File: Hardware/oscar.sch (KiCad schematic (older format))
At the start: 49 parts, among them J1 SWD_Header, J2 ChannelA_In, J3 ChannelB_In, J4 ChannelC_In, J5 ChA_Buff_Out, J6 ChB_Buff_Out, J7 ChC_Buff_Out, J8 MIDI_In, J9 Eurorack_10_pin_power, SW1 Left_Encoder, SW2 Right_Encoder, SW3 SW_Push, U1 STM32F446RETx, U2 ILI9341_SPI_Daughterboard, U3 MCP6004, U4 TL074, U5 LM1117-3.3, Y1 Crystal

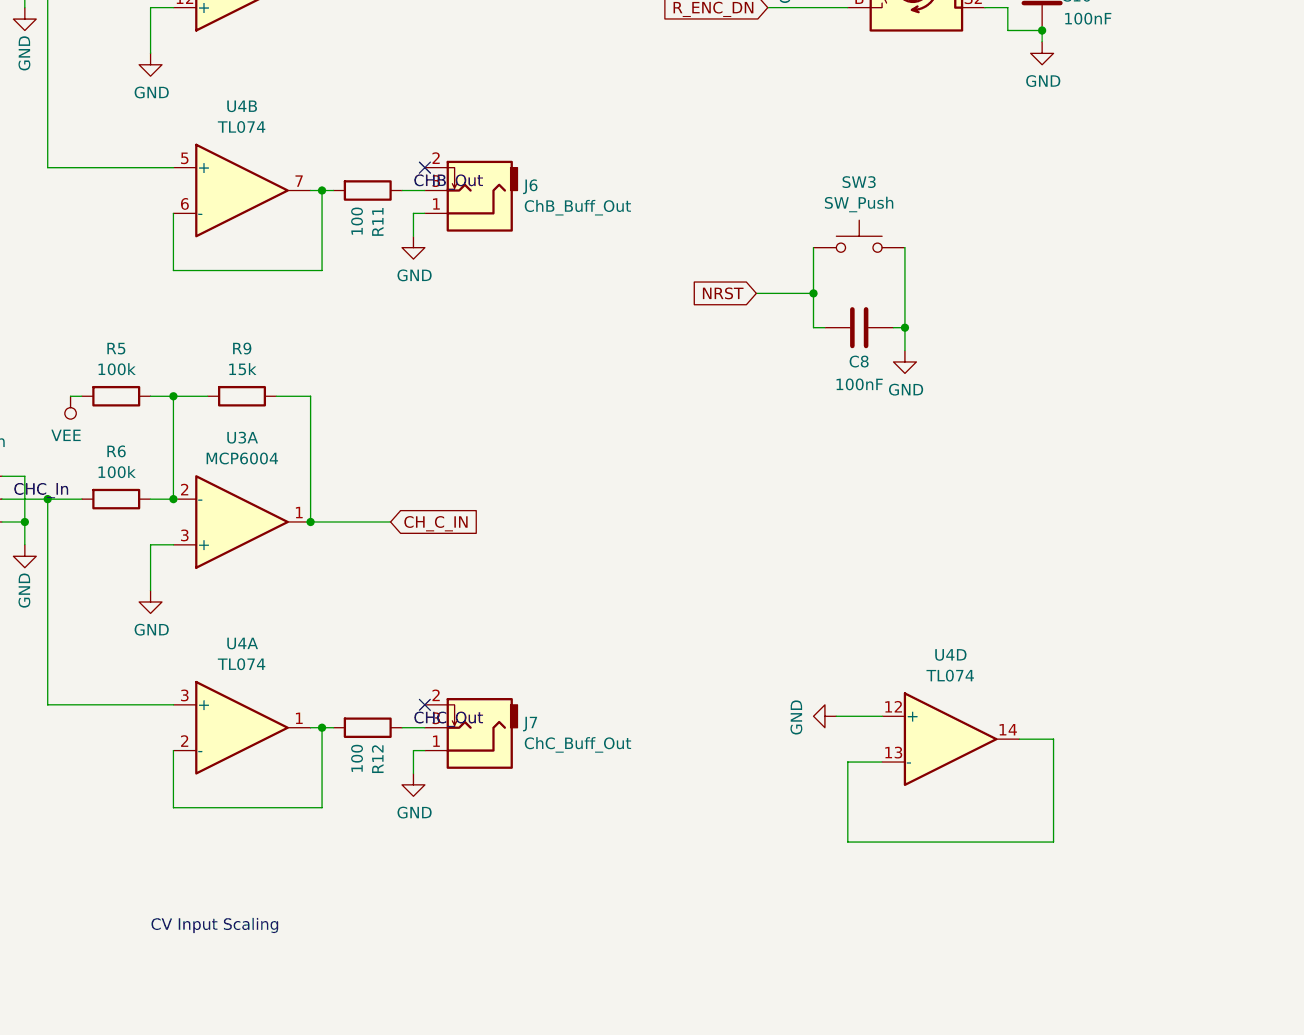
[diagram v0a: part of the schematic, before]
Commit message: Reorganised and relocated reposistory
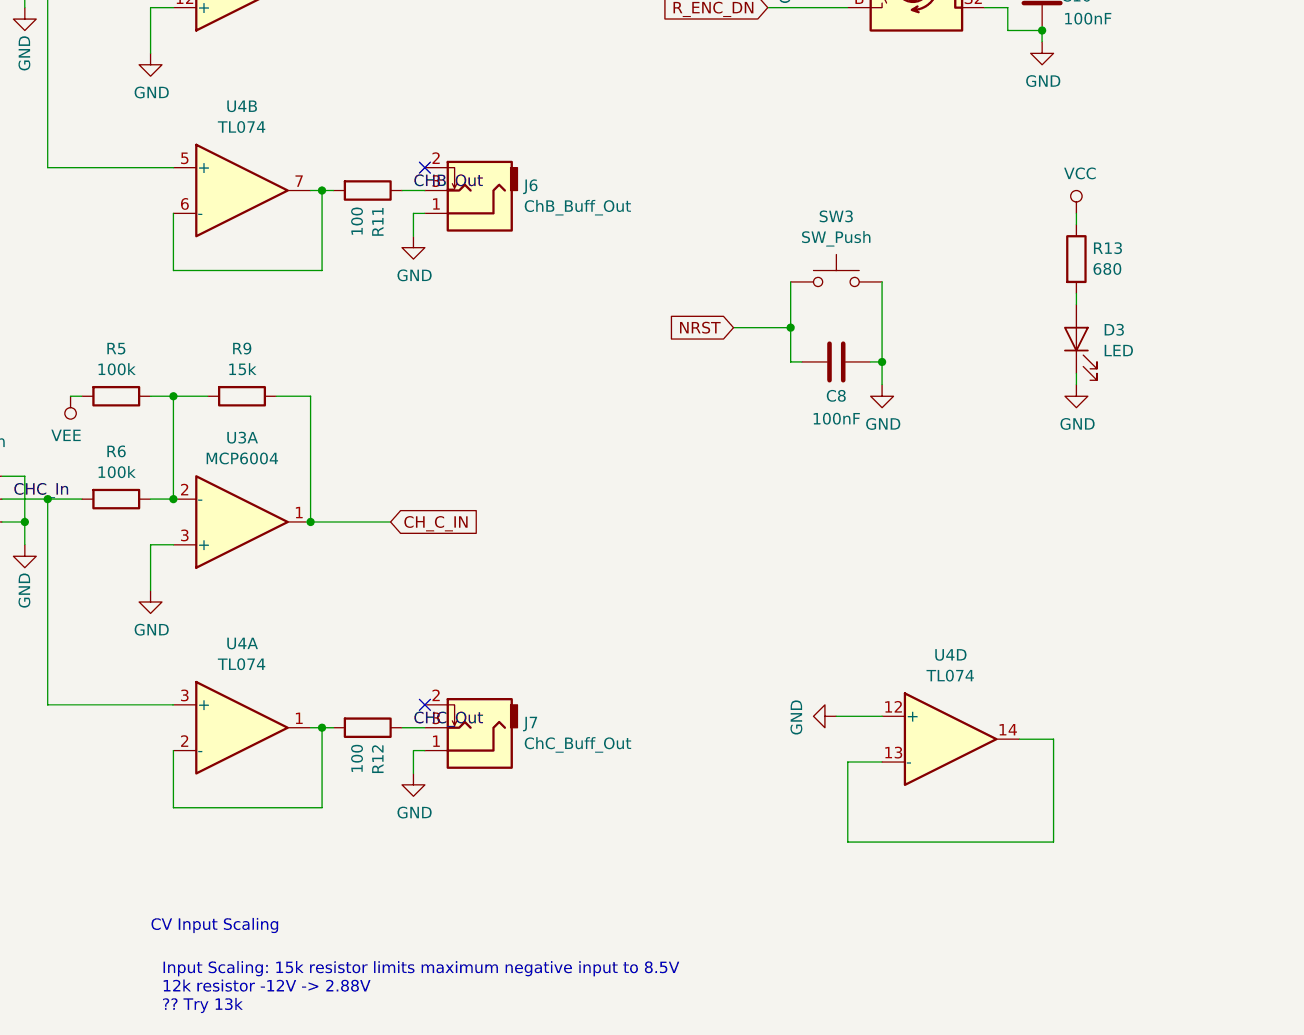
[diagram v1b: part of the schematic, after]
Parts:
- added D3: LED, LEDs:LED_D5.0mm, symbol Device:LED
- added R13: 680, Resistors_SMD:R_0805_HandSoldering, symbol Device:R
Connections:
- net GND: now also D3.1 (K)
- net VCC: now also R13.1
- new net: D3.2 (A), R13.2
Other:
- note added: "Input Scaling: 15k resistor limits maximum negative input to 8.5V\n12k resistor -12V -> 2.88V\n?? Try 13k"
- moved on the sheet: C8, SW3
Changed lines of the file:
@@
 Connection ~ 9550 3900
 Wire Wire Line
-	8550 4850 8550 5050
+	8450 5000 8450 5200
 $Comp
 L Device:C C8
 U 1 1 5D7D7D33
-P 8750 5200
-F 0 "C8" V 8900 5200 50  0000 C CNN
-F 1 "100nF" V 9000 5200 50  0000 C CNN
-F 2 "Capacitors_SMD:C_0805_HandSoldering" H 8788 5050 50  0001 C CNN
-F 3 "~" H 8750 5200 50  0001 C CNN
-	1    8750 5200
+P 8650 5350
+F 0 "C8" V 8800 5350 50  0000 C CNN
+F 1 "100nF" V 8900 5350 50  0000 C CNN
+F 2 "Capacitors_SMD:C_0805_HandSoldering" H 8688 5200 50  0001 C CNN
+F 3 "~" H 8650 5350 50  0001 C CNN
+	1    8650 5350
 	0    1    1    0
 $EndComp
 Wire Wire Line
-	8550 5050 8550 5200
-Wire Wire Line
-	8550 5200 8600 5200
-Connection ~ 8550 5050
-Wire Wire Line
-	8900 5200 8950 5200
-Wire Wire Line
-	8950 5200 8950 5300
-Connection ~ 8950 5200
+	8450 5200 8450 5350
+Wire Wire Line
+	8450 5350 8500 5350
+Connection ~ 8450 5200
+Wire Wire Line
+	8800 5350 8850 5350
+Wire Wire Line
+	8850 5350 8850 5450
+Connection ~ 8850 5350
 $Comp
 L power:GND #PWR028
 U 1 1 5D80DC54
-P 8950 5300
-F 0 "#PWR028" H 8950 5050 50  0001 C CNN
-F 1 "GND" H 8955 5127 50  0000 C CNN
-F 2 "" H 8950 5300 50  0001 C CNN
-F 3 "" H 8950 5300 50  0001 C CNN
-	1    8950 5300
-	1    0    0    -1
-$EndComp
-Text GLabel 8300 5050 0    50   Input ~ 0
+P 8850 5450
+F 0 "#PWR028" H 8850 5200 50  0001 C CNN
+F 1 "GND" H 8855 5277 50  0000 C CNN
+F 2 "" H 8850 5450 50  0001 C CNN
+F 3 "" H 8850 5450 50  0001 C CNN
+	1    8850 5450
+	1    0    0    -1
+$EndComp
+Text GLabel 8200 5200 0    50   Input ~ 0
 NRST
 Wire Wire Line
-	8300 5050 8550 5050
+	8200 5200 8450 5200
 Text GLabel 1650 2050 0    50   Input ~ 0
 NRST
@@
 L Switch:SW_Push SW3
 U 1 1 5D32F73D
-P 8750 4850
-F 0 "SW3" H 8750 5135 50  0000 C CNN
-F 1 "SW_Push" H 8750 5044 50  0000 C CNN
-F 2 "Buttons_Switches_THT:SW_PUSH_6mm" H 8750 5050 50  0001 C CNN
-F 3 "~" H 8750 5050 50  0001 C CNN
-	1    8750 4850
-	1    0    0    -1
-$EndComp
-Wire Wire Line
-	8950 4850 8950 5200
+P 8650 5000
+F 0 "SW3" H 8650 5285 50  0000 C CNN
+F 1 "SW_Push" H 8650 5194 50  0000 C CNN
+F 2 "Buttons_Switches_THT:SW_PUSH_6mm" H 8650 5200 50  0001 C CNN
+F 3 "~" H 8650 5200 50  0001 C CNN
+	1    8650 5000
+	1    0    0    -1
+$EndComp
+Wire Wire Line
+	8850 5000 8850 5350
 Text Label 5000 1450 0    50   ~ 0
 CHA_In
@@
 	0    -1   -1   0
 $EndComp
+$Comp
+L Device:R R13
+U 1 1 5D7C9628
+P 9700 4900
+F 0 "R13" H 9770 4946 50  0000 L CNN
+F 1 "680" H 9770 4855 50  0000 L CNN
+F 2 "Resistors_SMD:R_0805_HandSoldering" V 9630 4900 50  0001 C CNN
+F 3 "~" H 9700 4900 50  0001 C CNN
+	1    9700 4900
+	1    0    0    -1
+$EndComp
+$Comp
+L Device:LED D3
+U 1 1 5D7CAFA0
+P 9700 5250
+F 0 "D3" V 9739 5133 50  0000 R CNN
+F 1 "LED" V 9648 5133 50  0000 R CNN
+F 2 "LEDs:LED_D5.0mm" H 9700 5250 50  0001 C CNN
+F 3 "~" H 9700 5250 50  0001 C CNN
+	1    9700 5250
+	0    -1   -1   0
+$EndComp
+$Comp
+L power:GND #PWR08
+U 1 1 5D7CCDDA
+P 9700 5450
+F 0 "#PWR08" H 9700 5200 50  0001 C CNN
+F 1 "GND" H 9705 5277 50  0000 C CNN
+F 2 "" H 9700 5450 50  0001 C CNN
+F 3 "" H 9700 5450 50  0001 C CNN
+	1    9700 5450
+	1    0    0    -1
+$EndComp
+$Comp
+L power:VCC #PWR07
+U 1 1 5D7CDF44
+P 9700 4700
+F 0 "#PWR07" H 9700 4550 50  0001 C CNN
+F 1 "VCC" H 9717 4873 50  0000 C CNN
+F 2 "" H 9700 4700 50  0001 C CNN
+F 3 "" H 9700 4700 50  0001 C CNN
+	1    9700 4700
+	1    0    0    -1
+$EndComp
+Wire Wire Line
+	9700 4700 9700 4750
+Wire Wire Line
+	9700 5050 9700 5100
+Wire Wire Line
+	9700 5400 9700 5450
+Text Notes 5700 8200 0    50   ~ 0
+Input Scaling: 15k resistor limits maximum negative input to 8.5V\n12k resistor -12V -> 2.88V\n?? Try 13k
 $EndSCHEMATC

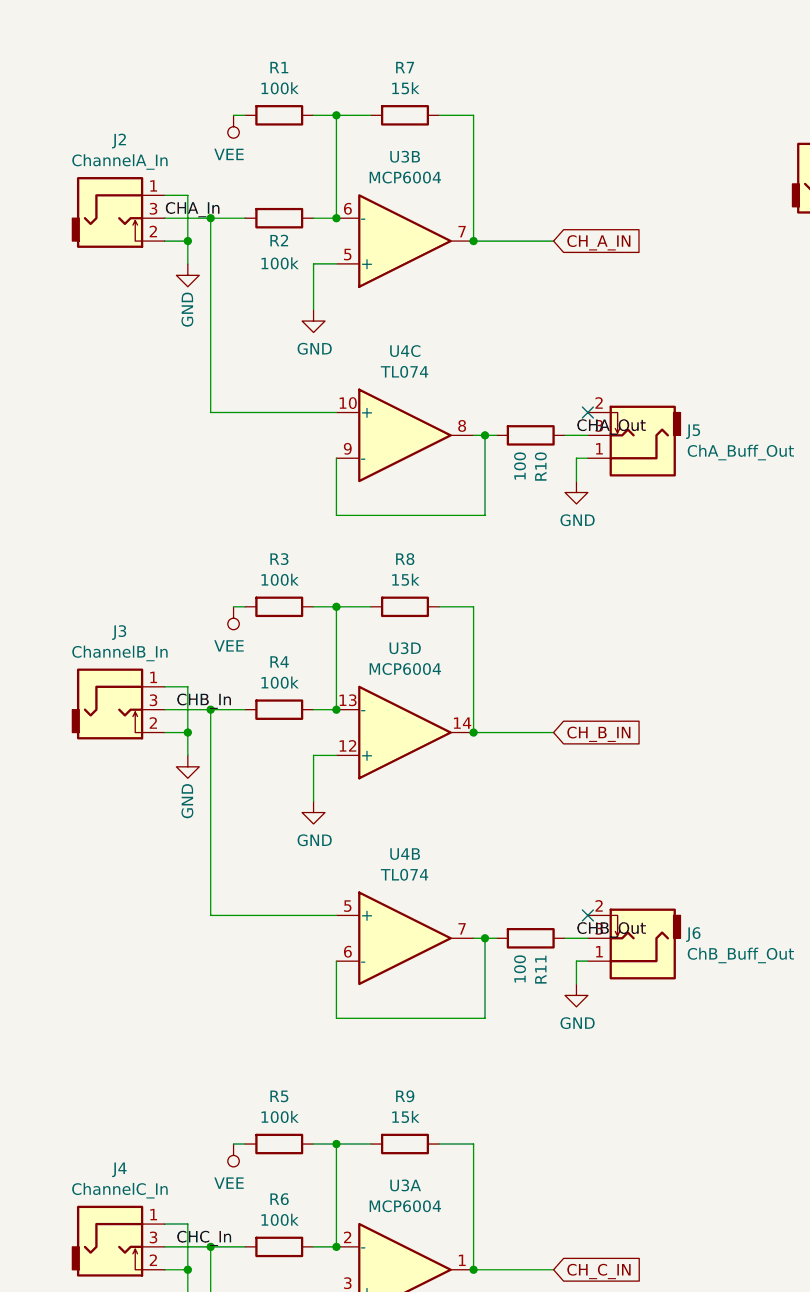
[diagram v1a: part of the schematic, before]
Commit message: Increased oscillator max voltage from 8V to 12V; fixes to FFT menu (allows channel select in config)
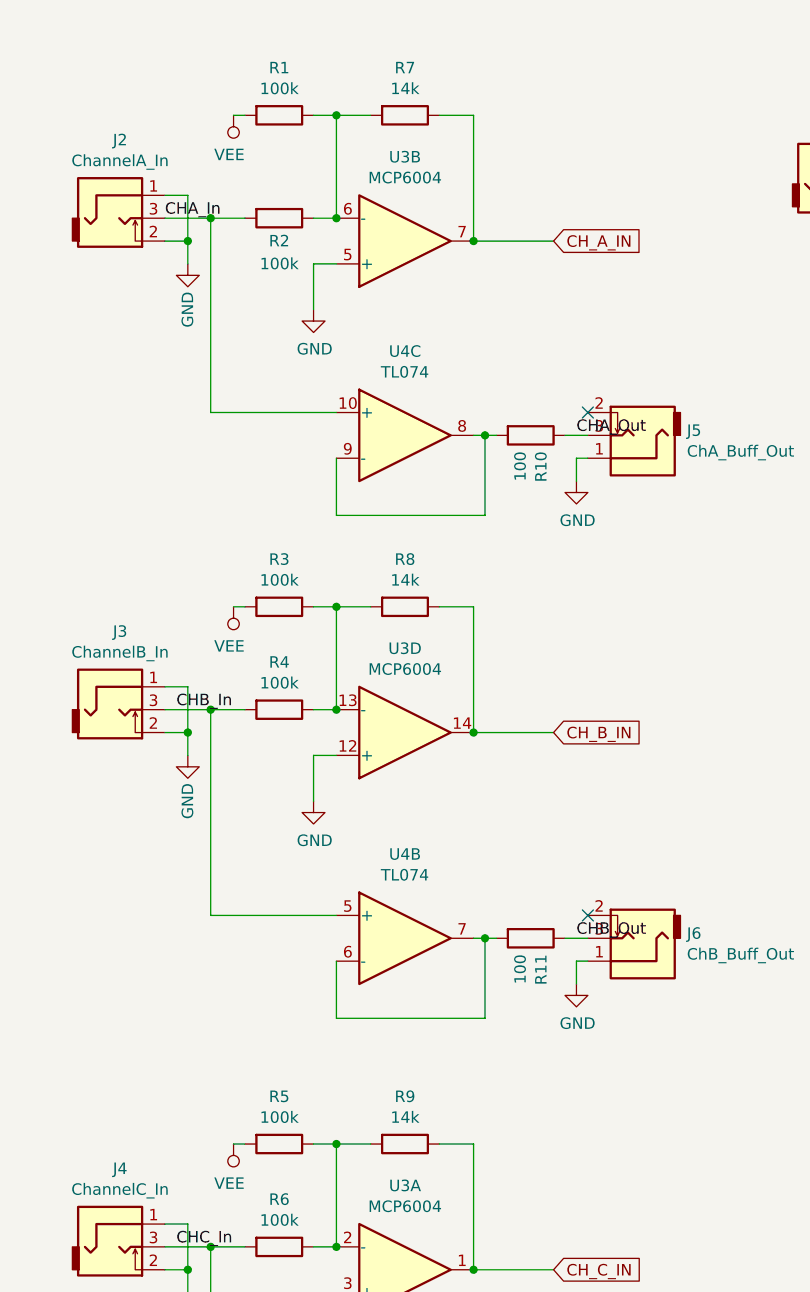
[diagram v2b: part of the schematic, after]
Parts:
- R7, R8, R9: value 15k -> 14k
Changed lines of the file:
@@
 P 6050 1000
 F 0 "R7" V 5843 1000 50  0000 C CNN
-F 1 "15k" V 5934 1000 50  0000 C CNN
+F 1 "14k" V 5934 1000 50  0000 C CNN
 F 2 "Resistors_SMD:R_0805_HandSoldering" V 5980 1000 50  0001 C CNN
 F 3 "~" H 6050 1000 50  0001 C CNN
@@
 P 6050 3150
 F 0 "R8" V 5843 3150 50  0000 C CNN
-F 1 "15k" V 5934 3150 50  0000 C CNN
+F 1 "14k" V 5934 3150 50  0000 C CNN
 F 2 "Resistors_SMD:R_0805_HandSoldering" V 5980 3150 50  0001 C CNN
 F 3 "~" H 6050 3150 50  0001 C CNN
@@
 P 6050 5500
 F 0 "R9" V 5843 5500 50  0000 C CNN
-F 1 "15k" V 5934 5500 50  0000 C CNN
+F 1 "14k" V 5934 5500 50  0000 C CNN
 F 2 "Resistors_SMD:R_0805_HandSoldering" V 5980 5500 50  0001 C CNN
 F 3 "~" H 6050 5500 50  0001 C CNN
